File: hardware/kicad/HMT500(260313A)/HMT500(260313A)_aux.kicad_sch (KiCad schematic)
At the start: 9 parts, among them Q1 MMBTA06

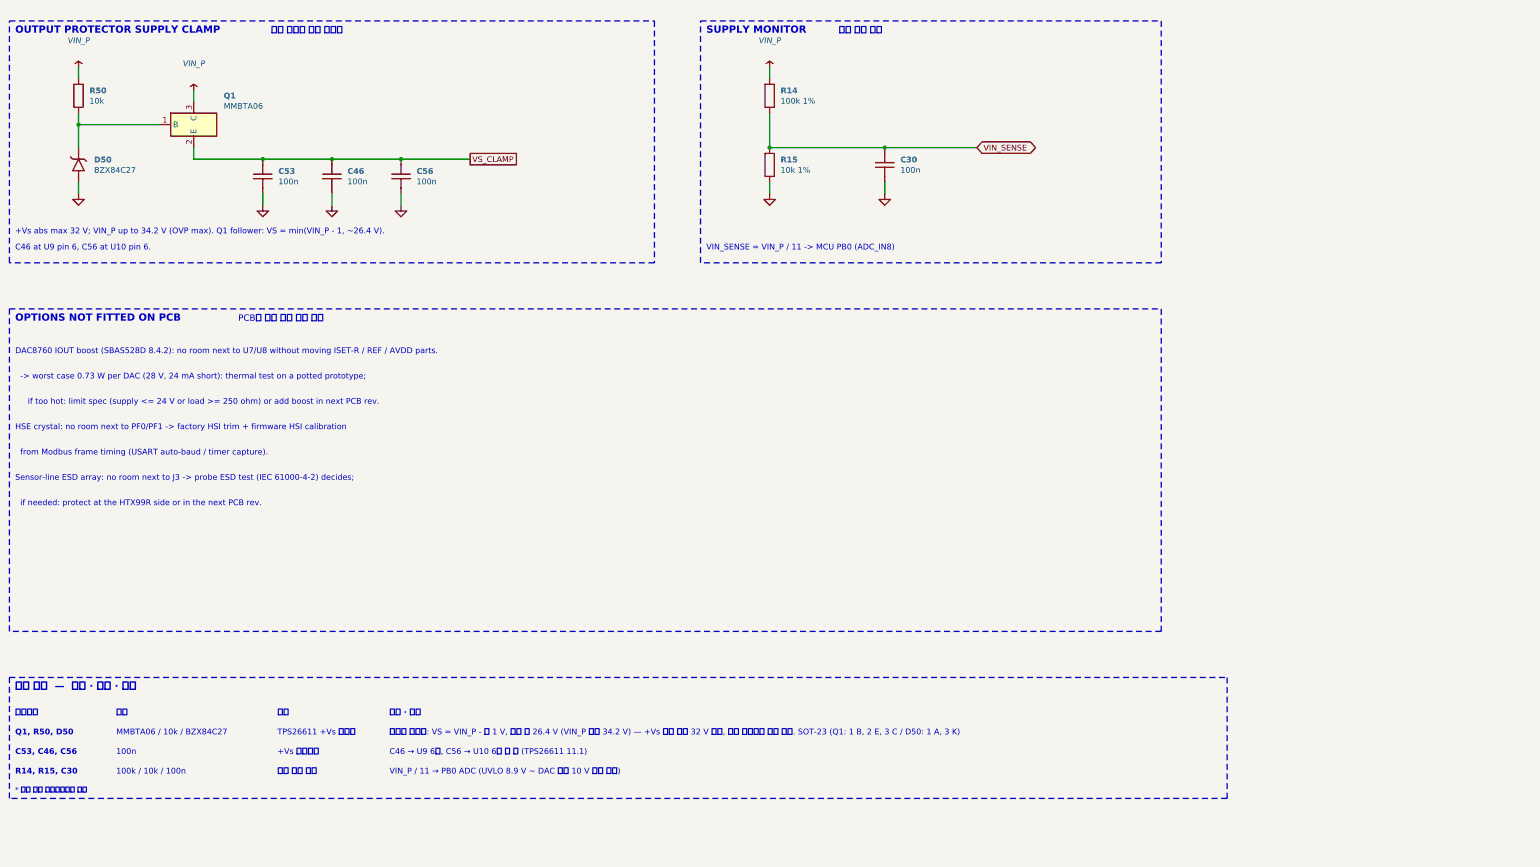
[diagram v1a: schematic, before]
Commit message: Apply agreed external review items (decision #35)
- H01: series 100 V Schottky D3 (PMEG10010ELR) between D2 and eFuse IN
  (new net VIN_D) so negative surges no longer stress U1 IN-OUT
- H02: RS-485 bus TVS D60/D61 (TVS3301); U11 -> THVD2410DGKR (VSSOP-8)
- H04: +Vs clamp zener 27 V -> 24 V (BZX84C24LT1G)
- H08: ADS1220 IDAC fixed at 250 uA
- Room for new parts: C7 removed, 37 low-voltage R/C moved to 0402
  (LCSC basic where available); chassis parts keep CH_GAP between each other
- Placement 104/104, netlist 78/78, pcbnew DRC: no clearance errors,
  assembly sim 23 OK; parts list / JLC BOM updated
- docs/hw/external-review-response-260930.md: item responses, output load
  table, current budget, firmware requirements F1-F6, tests T1-T7

Co-Authored-By: Claude Opus 5.5 <noreply@anthropic.com>
Claude-Session: https://claude.ai/code/session_01JA2o8uJsqp9Vzsg4b665ev
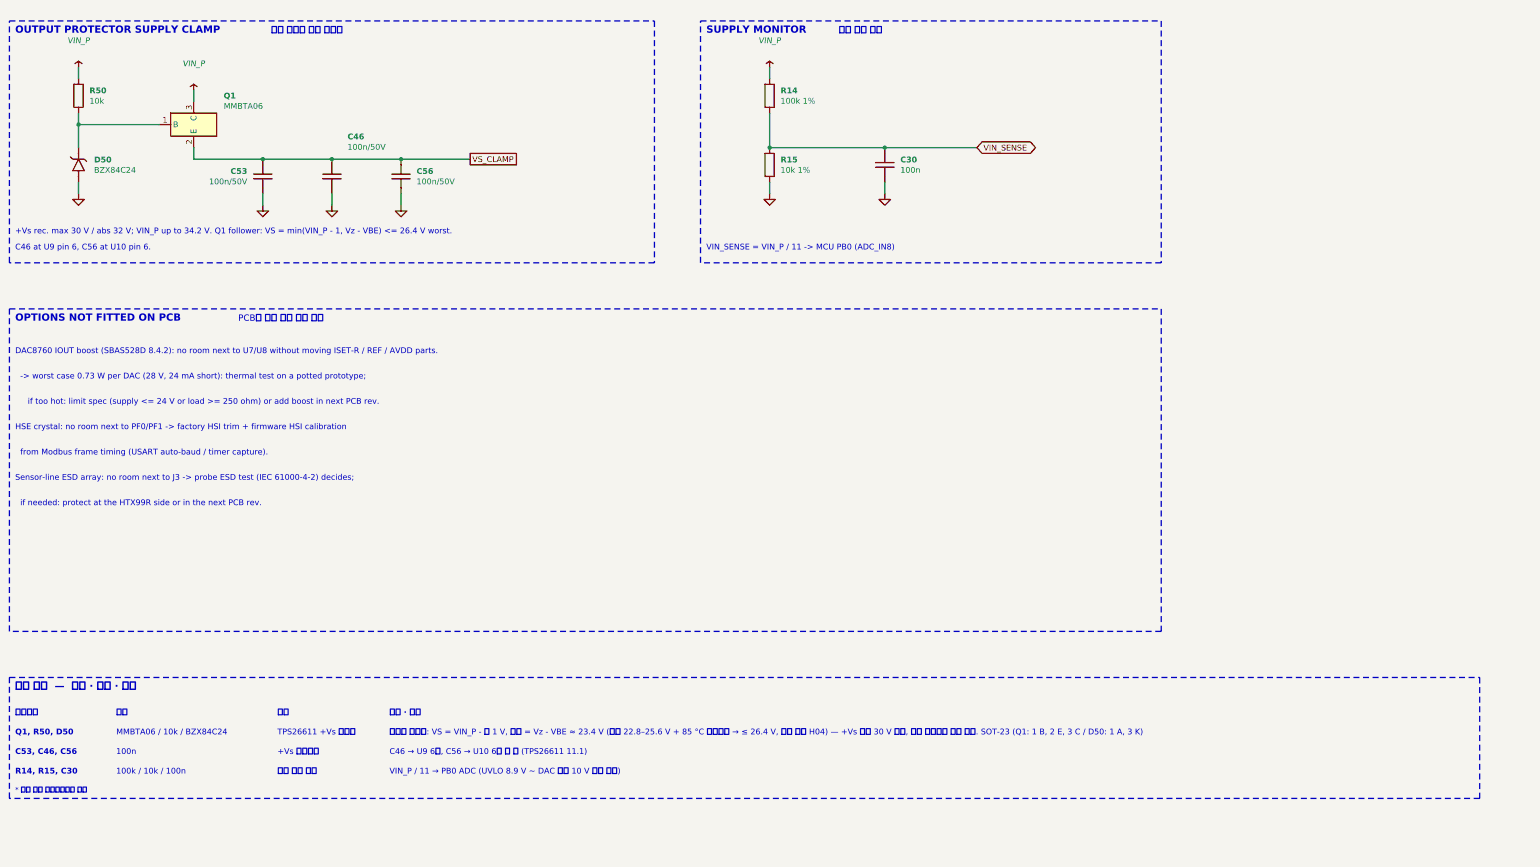
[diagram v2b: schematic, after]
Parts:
- C30: footprint Capacitor_SMD:C_0603_1608Metric -> Capacitor_SMD:C_0402_1005Metric
- C46, C53, C56: value 100n -> 100n/50V
- D50: value BZX84C27 -> BZX84C24
- R14, R15, R50: footprint Resistor_SMD:R_0603_1608Metric -> Resistor_SMD:R_0402_1005Metric
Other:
- note added: "+Vs rec. max 30 V / abs 32 V; VIN_P up to 34.2 V. Q1 follower: VS = min(VIN_P - 1, Vz - VBE) <= 26.4 V worst."
- note added: "MMBTA06 / 10k / BZX84C24"
- note added: "이미터 폴로워: VS = VIN_P - 약 1 V, 최대 = Vz - VBE ≈ 23.4 V (최악 22.8–25.6 V + 85 °C 드리프트 → ≤ 26.4 V, 외부 검수 H04) — +Vs 권장 30 V 여유, 낮은 전원에서 강하 작음. SOT-23 (Q1: 1 B, 2 E, 3 C / D50: 1 A, 3 K)"
- note removed: "+Vs abs max 32 V; VIN_P up to 34.2 V (OVP max). Q1 follower: VS = min(VIN_P - 1, ~26.4 V)."
- note removed: "MMBTA06 / 10k / BZX84C27"
- note removed: "이미터 폴로워: VS = VIN_P - 약 1 V, 최대 약 26.4 V (VIN_P 최대 34.2 V) — +Vs 절대 최대 32 V 보호, 낮은 전원에서 강하 작음. SOT-23 (Q1: 1 B, 2 E, 3 C / D50: 1 A, 3 K)"

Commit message: Decision #37: fix the DAC section with the IVS320 AO rev 1.0 scheme
- AO supply VAO 16.1 V: LMR51606YFDBVR buck (U15) + 22 uH + 2x10 uF,
  feeding DAC AVDD (via 10 ohm), TPS26611 +Vs and OPA197 V+
- Remove +Vs zener follower (Q1, R50, D50, C53) and C43
- DAC CMP compensation 4.7 nF VOUT-CMP + 100 pF CMP-GND (SBAS528D 8.3.2)
- DAC output clamp BAS70-04 (D41/D51) for protector switching transients
- Output TVS3301 and SGOOD -> MCU ADC kept (+-30 V miswiring requirement)
- 114/114 parts placed, netlist 82/82, DRC no clearance errors,
  assembly sim 23 OK; parts list, JLC BOM, review docs updated

Co-Authored-By: Claude Opus 5.5 <noreply@anthropic.com>
Claude-Session: https://claude.ai/code/session_01JA2o8uJsqp9Vzsg4b665ev
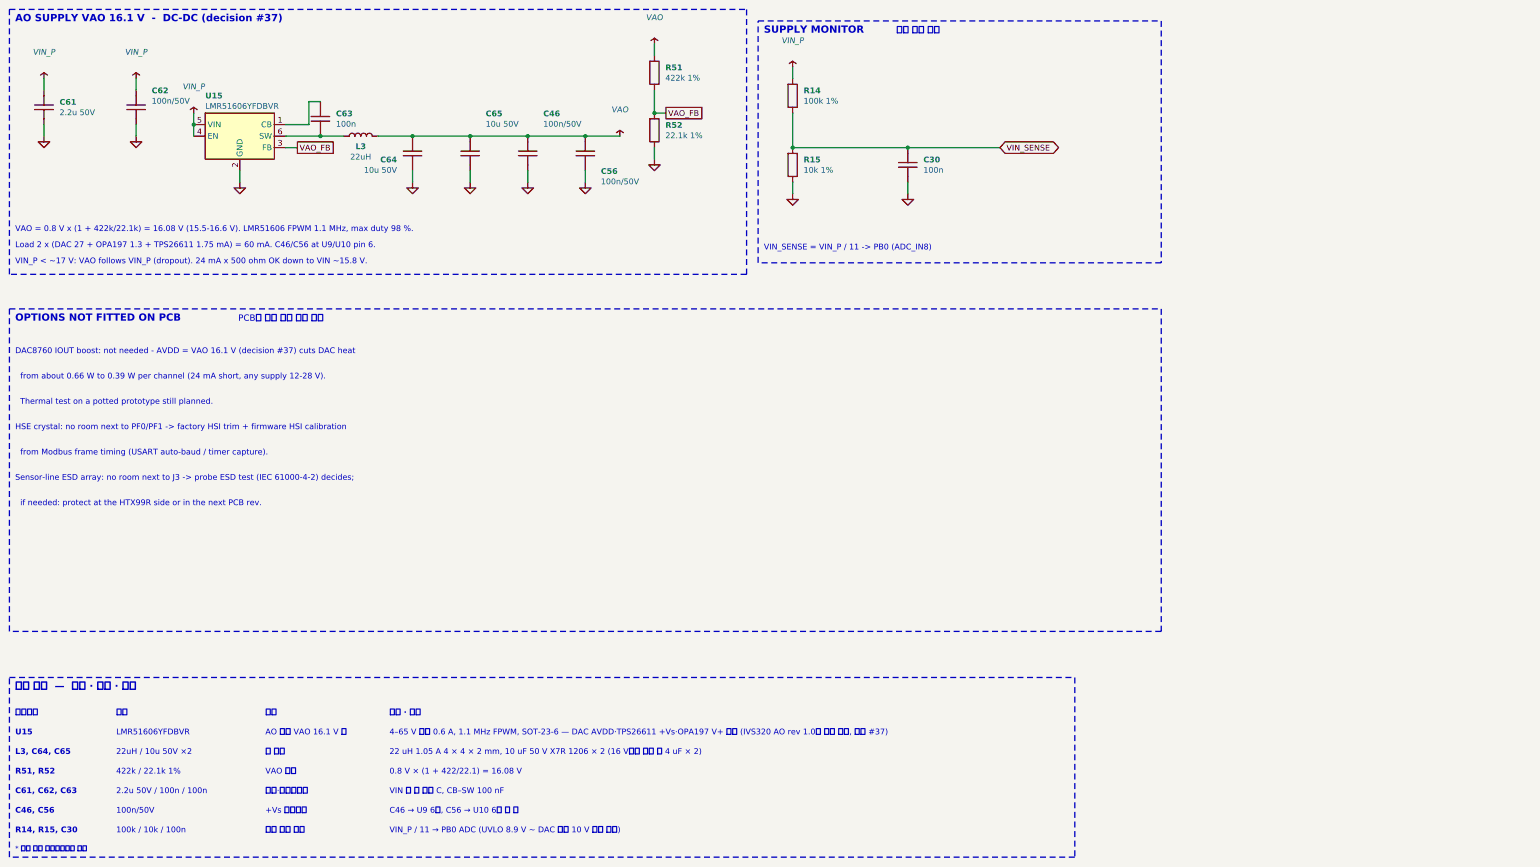
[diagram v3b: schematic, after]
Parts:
- removed C53: 100n/50V, Capacitor_SMD:C_0603_1608Metric, symbol HMT500_260313A:C
- removed D50: BZX84C24, Package_TO_SOT_SMD:SOT-23, symbol HMT500_260313A:ZENER
- removed Q1: MMBTA06, Package_TO_SOT_SMD:SOT-23, symbol HMT500_260313A:NPN_SOT23
- removed R50: 10k, Resistor_SMD:R_0402_1005Metric, symbol HMT500_260313A:R
- added C61: 2.2u 50V, Capacitor_SMD:C_0805_2012Metric, symbol HMT500_260313A:C
- added C62: 100n/50V, Capacitor_SMD:C_0603_1608Metric, symbol HMT500_260313A:C
- added C63: 100n, Capacitor_SMD:C_0402_1005Metric, symbol HMT500_260313A:C
- added C64, C65: 10u 50V, Capacitor_SMD:C_1206_3216Metric, symbol HMT500_260313A:C
- added L3: 22uH, Inductor_SMD:L_Taiyo-Yuden_NR-40xx, symbol HMT500_260313A:L
- added R51: 422k 1%, Resistor_SMD:R_0402_1005Metric, symbol HMT500_260313A:R
- added R52: 22.1k 1%, Resistor_SMD:R_0402_1005Metric, symbol HMT500_260313A:R
- added U15: LMR51606YFDBVR, Package_TO_SOT_SMD:SOT-23-6, symbol HMT500_260313A:LMR51606
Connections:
- net GND: now also C61.2, C62.2, C64.2, C65.2, R52.2, U15.2 (GND)
- net VIN_P: now also C61.1, C62.1, U15.4 (EN), U15.5 (VIN)
- net VS_CLAMP renamed VAO
- net VAO: now also C64.1, C65.1, L3.2, R51.1
- new net: C63.1, U15.1 (CB)
- new net: C63.2, L3.1, U15.6 (SW)
- new net VAO_FB: R51.2, R52.1, U15.3 (FB)
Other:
- note added: "0.8 V × (1 + 422/22.1) = 16.08 V"
- note added: "100n/50V"
- note added: "2.2u 50V / 100n / 100n"
- note added: "22 uH 1.05 A 4 × 4 × 2 mm, 10 uF 50 V X7R 1206 × 2 (16 V에서 실효 약 4 uF × 2)"
- note added: "22uH / 10u 50V ×2"
- note added: "422k / 22.1k 1%"
- note added: "4–65 V 입력 0.6 A, 1.1 MHz FPWM, SOT-23-6 — DAC AVDD·TPS26611 +Vs·OPA197 V+ 공용 (IVS320 AO rev 1.0과 같은 회로, 결정 #37)"
- note added: "AO SUPPLY VAO 16.1 V - DC-DC (decision #37)"
- note added: "AO 전원 VAO 16.1 V 벅"
- note added: "C46 → U9 6번, C56 → U10 6번 핀 옆"
- note added: "C46, C56"
- note added: "C61, C62, C63"
- note added: "DAC8760 IOUT boost: not needed - AVDD = VAO 16.1 V (decision #37) cuts DAC heat"
- note added: "L3, C64, C65"
- note added: "LMR51606YFDBVR"
- note added: "Load 2 x (DAC 27 + OPA197 1.3 + TPS26611 1.75 mA) = 60 mA. C46/C56 at U9/U10 pin 6."
- note added: "R51, R52"
- note added: "Thermal test on a potted prototype still planned."
- note added: "U15"
- note added: "VAO = 0.8 V x (1 + 422k/22.1k) = 16.08 V (15.5-16.6 V). LMR51606 FPWM 1.1 MHz, max duty 98 %."
- note added: "VAO 설정"
- note added: "VIN 핀 옆 입력 C, CB–SW 100 nF"
- note added: "VIN_P < ~17 V: VAO follows VIN_P (dropout). 24 mA x 500 ohm OK down to VIN ~15.8 V."
- note added: "VIN_SENSE = VIN_P / 11 -> PB0 (ADC_IN8)"
- note added: "from about 0.66 W to 0.39 W per channel (24 mA short, any supply 12-28 V)."
- note added: "벅 출력"
- note added: "입력·부트스트랩"
- note removed: "+Vs rec. max 30 V / abs 32 V; VIN_P up to 34.2 V. Q1 follower: VS = min(VIN_P - 1, Vz - VBE) <= 26.4 V worst."
- note removed: "-> worst case 0.73 W per DAC (28 V, 24 mA short): thermal test on a potted prototype;"
- note removed: "100n"
- note removed: "C46 at U9 pin 6, C56 at U10 pin 6."
- note removed: "C46 → U9 6번, C56 → U10 6번 핀 옆 (TPS26611 11.1)"
- note removed: "C53, C46, C56"
- note removed: "DAC8760 IOUT boost (SBAS528D 8.4.2): no room next to U7/U8 without moving ISET-R / REF / AVDD parts."
- note removed: "MMBTA06 / 10k / BZX84C24"
- note removed: "OUTPUT PROTECTOR SUPPLY CLAMP"
- note removed: "Q1, R50, D50"
- note removed: "TPS26611 +Vs 클램프"
- note removed: "VIN_SENSE = VIN_P / 11 -> MCU PB0 (ADC_IN8)"
- note removed: "if too hot: limit spec (supply <= 24 V or load >= 250 ohm) or add boost in next PCB rev."
- note removed: "이미터 폴로워: VS = VIN_P - 약 1 V, 최대 = Vz - VBE ≈ 23.4 V (최악 22.8–25.6 V + 85 °C 드리프트 → ≤ 26.4 V, 외부 검수 H04) — +Vs 권장 30 V 여유, 낮은 전원에서 강하 작음. SOT-23 (Q1: 1 B, 2 E, 3 C / D50: 1 A, 3 K)"
- note removed: "출력 보호기 전원 클램프"
- moved on the sheet: C30, C46, C56, R14, R15
